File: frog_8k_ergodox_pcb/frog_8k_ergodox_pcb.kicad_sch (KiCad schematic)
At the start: 24 parts, among them J1 USB_C_Receptacle_USB2.0_14P, SW1 SW_DPST_x2, SW2 SW_DPST_x2, U1 PMW3360DM-T2QU, U2 STM32F072CBTx, U3 TLV74318PDBVR

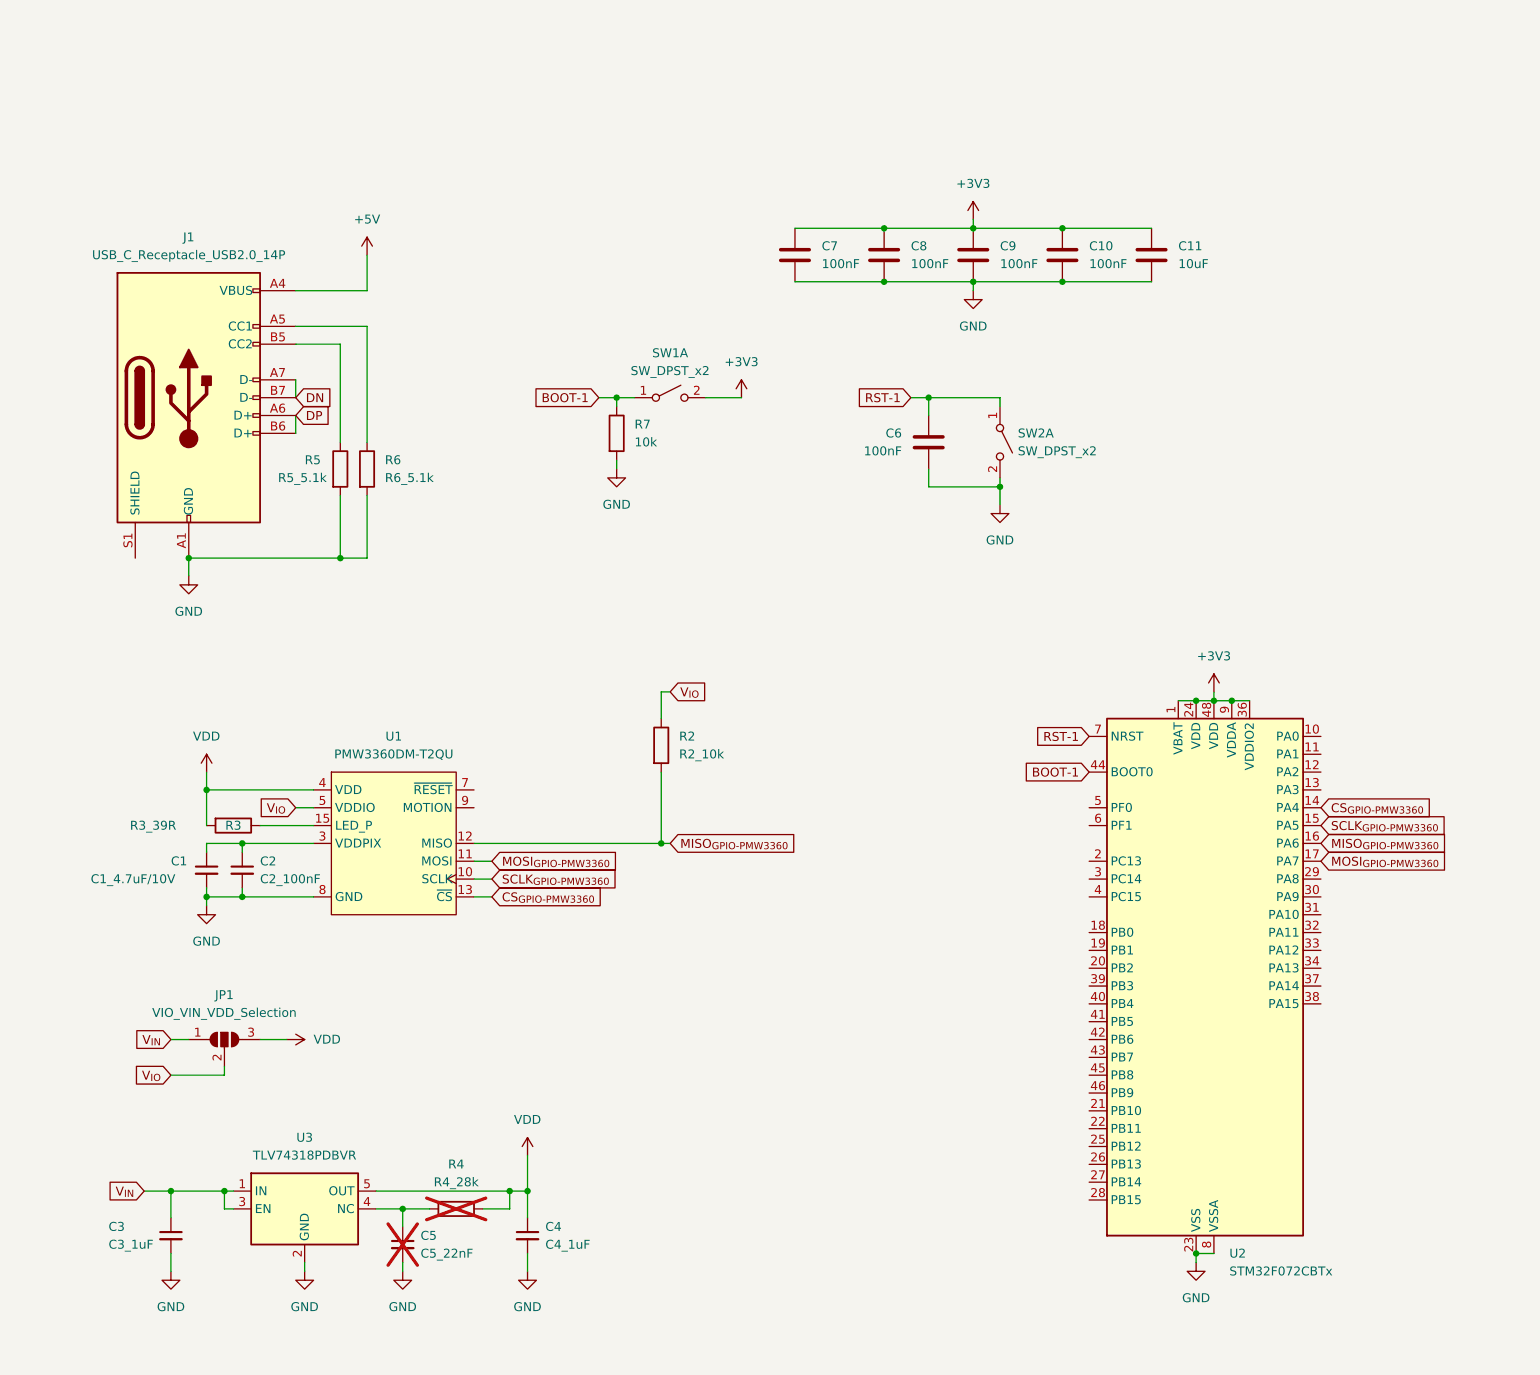
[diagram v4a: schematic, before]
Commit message: Removed unused symbol in PMW3360, Added Regulator for PCB
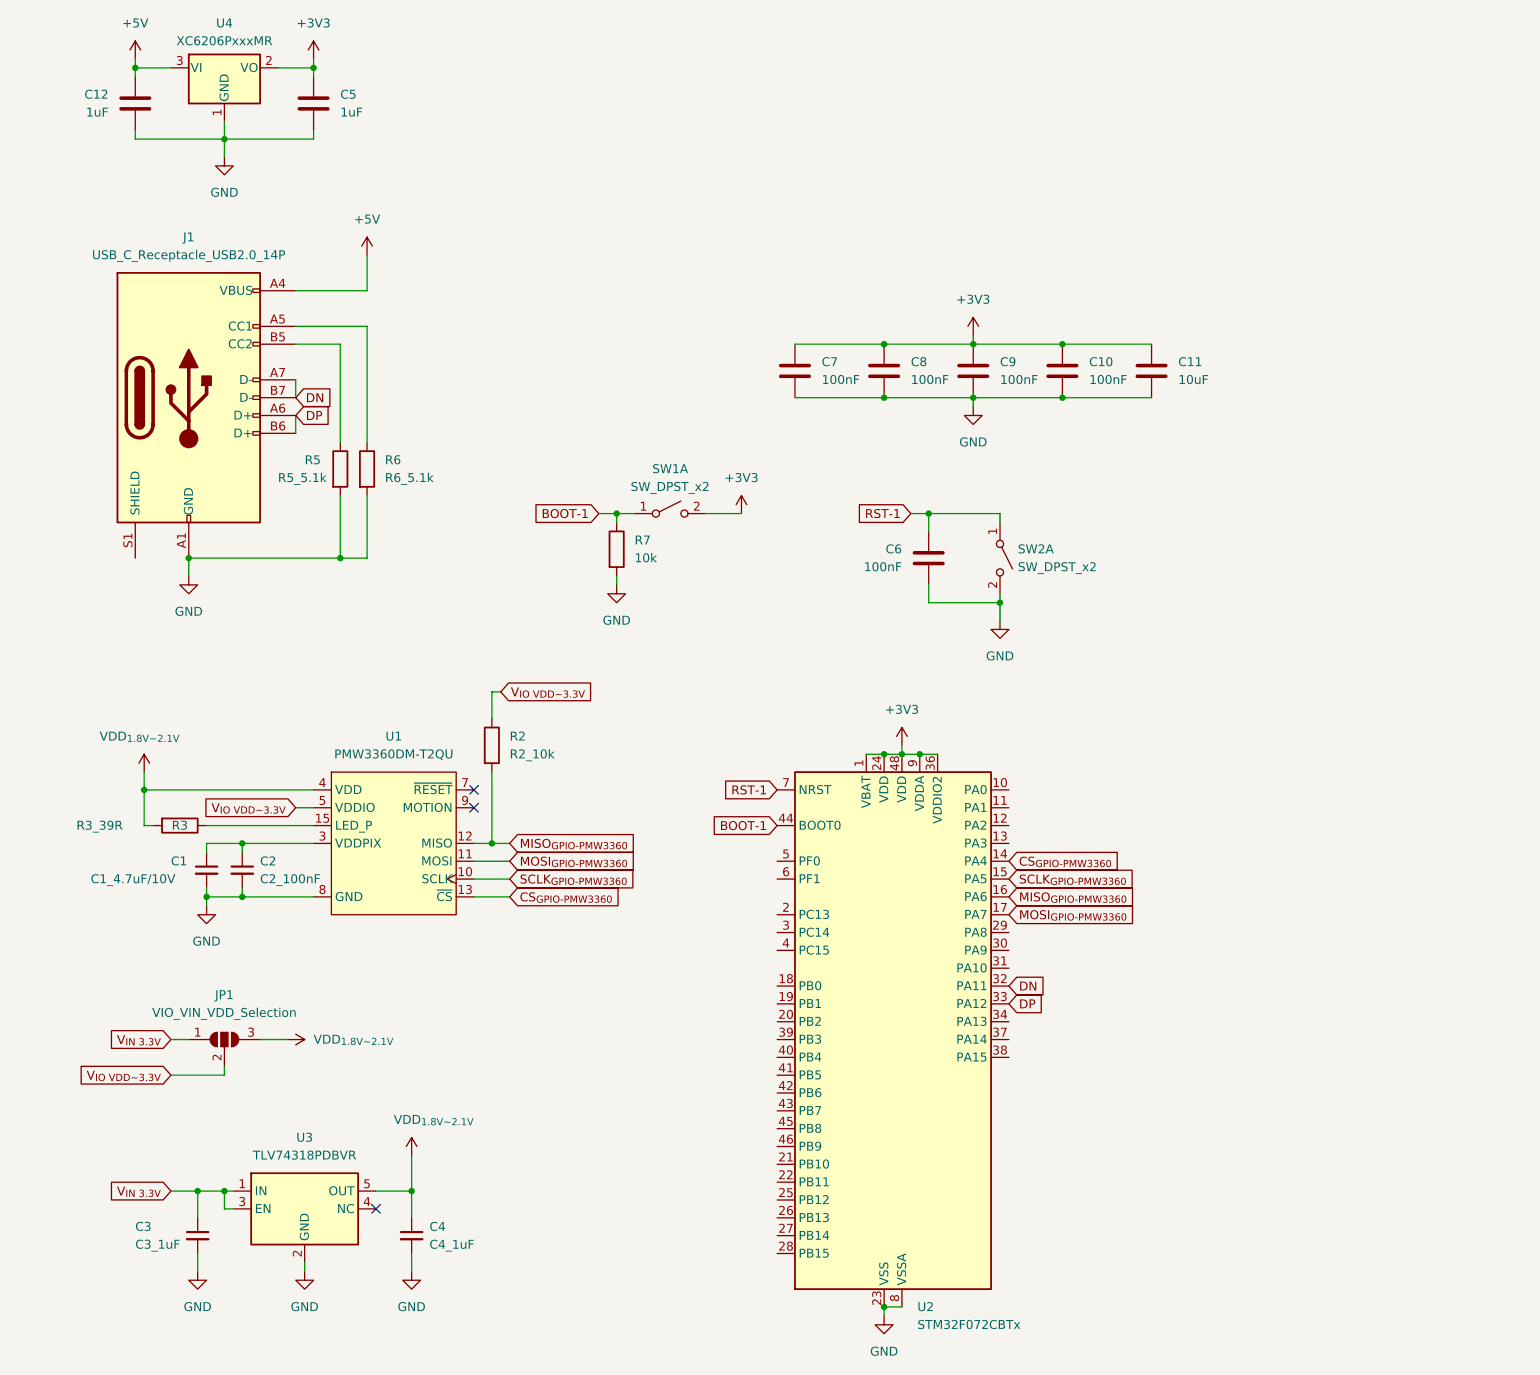
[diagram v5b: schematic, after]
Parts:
- removed C5: C5_22nF, Capacitor_SMD:C_0805_2012Metric_Pad1.18x1.45mm_HandSolder, symbol Device:C_Small
- removed R4: R4_28k, Resistor_SMD:R_0805_2012Metric_Pad1.20x1.40mm_HandSolder, symbol Device:R
- added C12, C5: 1uF, Capacitor_SMD:C_0402_1005Metric, symbol Device:C
- added U4: XC6206PxxxMR, Package_TO_SOT_SMD:SOT-23-3, symbol Regulator_Linear:XC6206PxxxMR
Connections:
- net +3V3: now also C5.1, U4.2 (VO)
- net +5V: now also C12.1, U4.3 (VI)
- net DN: now also U2.32 (PA11)
- net DP: now also U2.33 (PA12)
- net GND: now also C12.2, C5.2, U4.1 (GND)
- net VDD renamed VDD_{1.8V~2.1V}
- net V_{IN} renamed V_{IN 3.3V}
- net V_{IO} renamed V_{IO VDD~3.3V}
- no-connect marks 0 -> 3
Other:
- moved on the sheet: C10, C11, C3, C4, C6, C7, C8, C9, R2, R3, R7, SW1A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

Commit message: Added Switches and JST connector.
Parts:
- removed JP1: VIO_VIN_VDD_Selection, Jumper:SolderJumper-3_P1.3mm_Open_RoundedPad1.0x1.5mm_NumberLabels, symbol Jumper:SolderJumper_3_Open
- added J2: Conn_01x04_Pin, Connector_JST:JST_SH_SM04B-SRSS-TB_1x04-1MP_P1.00mm_Horizontal, symbol Connector:Conn_01x04_Pin
- added MX1, MX10, MX11, MX12, MX13, MX14, MX15, MX16, MX17, MX18, MX19, MX2, MX20, MX21, MX22, MX23, MX24, MX25, MX26, MX27, MX28, MX29, MX3, MX30, MX31, MX32, MX33, MX34, MX35, MX36, MX37, MX38, MX39, MX4, MX40, MX41, MX42, MX43, MX44, MX45, MX46, MX47, MX48, MX49, MX5, MX50, MX51, MX52, MX53, MX54, MX55, MX56, MX57, MX58, MX59, MX6, MX60, MX61, MX62, MX63, MX64, MX65, MX66, MX67, MX68, MX69, MX7, MX70, MX71, MX72, MX73, MX74, MX75, MX76, MX77, MX78, MX79, MX8, MX80, MX81, MX82, MX83, MX84, MX85, MX86, MX87, MX88, MX9: MX_SW_solder, PCM_marbastlib-mx:SW_MX_1u, symbol PCM_marbastlib-mx:MX_SW_solder
- J1: footprint (none) -> Connector_JST:JST_SH_SM04B-SRSS-TB_1x04-1MP_P1.00mm_Horizontal
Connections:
- net +5V: now also J2.1 (Pin_1)
- net DN: now also J2.2 (Pin_2)
- net DP: now also J2.3 (Pin_3)
- net GND: now also J2.4 (Pin_4)
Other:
- moved on the sheet: C1, C10, C11, C12, C2, C3, C4, C5, C6, C7, C8, C9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

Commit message: Updated Matrix & Col2Row Based Diodes.
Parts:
- added D1, D10, D11, D12, D13, D14, D15, D16, D17, D18, D19, D2, D20, D21, D22, D23, D24, D25, D26, D27, D28, D29, D3, D30, D31, D32, D33, D34, D35, D36, D37, D38, D39, D4, D40, D41, D42, D43, D44, D45, D46, D47, D48, D49, D5, D50, D51, D52, D53, D54, D55, D56, D57, D58, D59, D6, D60, D61, D62, D63, D64, D65, D66, D67, D68, D69, D7, D70, D71, D72, D73, D74, D75, D76, D77, D78, D79, D8, D80, D81, D82, D83, D84, D85, D86, D87, D88, D9: 1N4148, Diode_SMD:D_SOD-123, symbol Device:D
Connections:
- net COL8: now reaches MX39.1
- net COL8: now also MX25.1, MX53.1, MX65.1, MX8.1, MX81.1, U2.45 (PB8)
- net at MX39.2: now also D39.2 (A)
- net COL1: now reaches MX46.1
- net COL1: now also MX18.1, MX32.1, MX60.1, U2.19 (PB1)
- net at MX46.2: now also D46.2 (A)
- net COL12: now reaches MX69.1
- net COL12: now also MX12.1, MX29.1, MX43.1, MX57.1, U2.25 (PB12)
- net at MX69.2: now also D69.2 (A)
- net COL7: now reaches MX38.1
- net COL7: now also MX24.1, MX52.1, MX7.1, MX80.1, U2.43 (PB7)
- net at MX38.2: now also D38.2 (A)
- net at MX52.2: now also D52.2 (A)
- net COL14: now reaches MX86.1
- net COL14: now also MX14.1, MX71.1, U2.27 (PB14)
- net at MX86.2: now also D86.2 (A)
- net COL2: now reaches MX47.1
- net COL2: now also MX19.1, MX2.1, MX33.1, MX61.1, MX75.1, U2.20 (PB2)
- net at MX47.2: now also D47.2 (A)
- net COL10: now reaches MX67.1
- net COL10: now also MX10.1, MX27.1, MX41.1, MX55.1, MX83.1, U2.21 (PB10)
- net at MX67.2: now also D67.2 (A)
- net COL15: now reaches MX15.1
- net COL15: now also MX72.1, MX87.1, U2.28 (PB15)
- net at MX15.2: now also D15.2 (A)
- net COL13: now reaches MX85.1
- net COL13: now also MX13.1, MX30.1, MX44.1, MX58.1, MX70.1, U2.26 (PB13)
- net at MX85.2: now also D85.2 (A)
- net COL6: now reaches MX37.1
- net COL6: now also MX23.1, MX51.1, MX6.1, MX79.1, U2.42 (PB6)
- net at MX37.2: now also D37.2 (A)
- net at MX87.2: now also D87.2 (A)
- net at MX30.2: now also D30.2 (A)
- net COL0: now reaches MX45.1
- net COL0: now also MX1.1, MX17.1, MX31.1, MX59.1, MX74.1, U2.18 (PB0)
- net at MX45.2: now also D45.2 (A)
- net COL16: now reaches U2.10 (PA0)
- net COL16: now also MX16.1, MX73.1, MX88.1
- net ROW2: now reaches U2.2 (PC13)
- net ROW2: now also D31.1 (K), D32.1 (K), D33.1 (K), D34.1 (K), D35.1 (K), D36.1 (K), D37.1 (K), D38.1 (K), D39.1 (K), D40.1 (K), D41.1 (K), D42.1 (K), D43.1 (K), D44.1 (K)
- net COL11: now reaches U2.22 (PB11)
- net COL11: now also MX11.1, MX28.1, MX42.1, MX56.1, MX68.1, MX84.1
- net ROW3: now reaches U2.3 (PC14)
- net ROW3: now also D45.1 (K), D46.1 (K), D47.1 (K), D48.1 (K), D49.1 (K), D50.1 (K), D51.1 (K), D52.1 (K), D53.1 (K), D54.1 (K), D55.1 (K), D56.1 (K), D57.1 (K), D58.1 (K)
- net ROW5: now reaches U2.38 (PA15)
- net ROW5: now also D74.1 (K), D75.1 (K), D76.1 (K), D77.1 (K), D78.1 (K), D79.1 (K), D80.1 (K), D81.1 (K), D82.1 (K), D83.1 (K), D84.1 (K), D85.1 (K), D86.1 (K), D87.1 (K), D88.1 (K)
- net COL3: now reaches U2.39 (PB3)
- net COL3: now also MX20.1, MX3.1, MX34.1, MX48.1, MX62.1, MX76.1
- net ROW4: now reaches U2.4 (PC15)
- net ROW4: now also D59.1 (K), D60.1 (K), D61.1 (K), D62.1 (K), D63.1 (K), D64.1 (K), D65.1 (K), D66.1 (K), D67.1 (K), D68.1 (K), D69.1 (K), D70.1 (K), D71.1 (K), D72.1 (K), D73.1 (K)
- net COL4: now reaches U2.40 (PB4)
- net COL4: now also MX21.1, MX35.1, MX4.1, MX49.1, MX63.1, MX77.1
- net COL5: now reaches U2.41 (PB5)
- net COL5: now also MX22.1, MX36.1, MX5.1, MX50.1, MX64.1, MX78.1
- net COL9: now reaches U2.46 (PB9)
- net COL9: now also MX26.1, MX40.1, MX54.1, MX66.1, MX82.1, MX9.1
- net ROW0: now reaches U2.5 (PF0)
- net ROW0: now also D1.1 (K), D10.1 (K), D11.1 (K), D12.1 (K), D13.1 (K), D14.1 (K), D15.1 (K), D16.1 (K), D2.1 (K), D3.1 (K), D4.1 (K), D5.1 (K), D6.1 (K), D7.1 (K), D8.1 (K), D9.1 (K)
- net ROW1: now reaches U2.6 (PF1)
- net ROW1: now also D17.1 (K), D18.1 (K), D19.1 (K), D20.1 (K), D21.1 (K), D22.1 (K), D23.1 (K), D24.1 (K), D25.1 (K), D26.1 (K), D27.1 (K), D28.1 (K), D29.1 (K), D30.1 (K)
- net at MX34.2: now also D34.2 (A)
- net at MX57.2: now also D57.2 (A)
- net at MX82.2: now also D82.2 (A)
- net at MX35.2: now also D35.2 (A)
- net at MX22.2: now also D22.2 (A)
- net at MX10.2: now also D10.2 (A)
- net at MX62.2: now also D62.2 (A)
- net at MX49.2: now also D49.2 (A)
- net at MX11.2: now also D11.2 (A)
- net at MX13.2: now also D13.2 (A)
- net at MX9.2: now also D9.2 (A)
- net at MX28.2: now also D28.2 (A)
- net at MX41.2: now also D41.2 (A)
- net at MX23.2: now also D23.2 (A)
- net at MX17.2: now also D17.2 (A)
- net at MX55.2: now also D55.2 (A)
- net at MX77.2: now also D77.2 (A)
- net at MX63.2: now also D63.2 (A)
- net at MX19.2: now also D19.2 (A)
- net at MX74.2: now also D74.2 (A)
- net at MX60.2: now also D60.2 (A)
- net at MX51.2: now also D51.2 (A)
- net at MX6.2: now also D6.2 (A)
- net at MX70.2: now also D70.2 (A)
- net at MX68.2: now also D68.2 (A)
- net at MX65.2: now also D65.2 (A)
- net at MX26.2: now also D26.2 (A)
- net at MX59.2: now also D59.2 (A)
- net at MX43.2: now also D43.2 (A)
- net at MX76.2: now also D76.2 (A)
- net at MX48.2: now also D48.2 (A)
- net at MX4.2: now also D4.2 (A)
- net at MX3.2: now also D3.2 (A)
- net at MX54.2: now also D54.2 (A)
- net at MX27.2: now also D27.2 (A)
- net at MX40.2: now also D40.2 (A)
- net at MX2.2: now also D2.2 (A)
- net at MX79.2: now also D79.2 (A)
- net at MX14.2: now also D14.2 (A)
- net at MX61.2: now also D61.2 (A)
- net at MX50.2: now also D50.2 (A)
- net at MX36.2: now also D36.2 (A)
- net at MX12.2: now also D12.2 (A)
- net at MX20.2: now also D20.2 (A)
- net at MX7.2: now also D7.2 (A)
- net at MX84.2: now also D84.2 (A)
- net at MX56.2: now also D56.2 (A)
- net at MX58.2: now also D58.2 (A)
- net at MX83.2: now also D83.2 (A)
- net at MX1.2: now also D1.2 (A)
- net at MX88.2: now also D88.2 (A)
- net at MX75.2: now also D75.2 (A)
- net at MX42.2: now also D42.2 (A)
- net at MX71.2: now also D71.2 (A)
- net at MX18.2: now also D18.2 (A)
- net at MX31.2: now also D31.2 (A)
- net at MX24.2: now also D24.2 (A)
- net at MX81.2: now also D81.2 (A)
- net at MX73.2: now also D73.2 (A)
- net at MX33.2: now also D33.2 (A)
- net at MX8.2: now also D8.2 (A)
- net at MX16.2: now also D16.2 (A)
- net at MX64.2: now also D64.2 (A)
- net at MX53.2: now also D53.2 (A)
- net at MX78.2: now also D78.2 (A)
- net at MX72.2: now also D72.2 (A)
- net at MX29.2: now also D29.2 (A)
- net at MX25.2: now also D25.2 (A)
- net at MX44.2: now also D44.2 (A)
- net at MX5.2: now also D5.2 (A)
- net at MX80.2: now also D80.2 (A)
- net at MX32.2: now also D32.2 (A)
- net at MX66.2: now also D66.2 (A)
- net at MX21.2: now also D21.2 (A)
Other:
- moved on the sheet: C1, C10, C11, C12, C2, C3, C4, C5, C6, C7, C8, C9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
